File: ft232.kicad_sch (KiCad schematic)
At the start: 0 parts

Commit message: Add components: TXS0108E, FT232 oscillators/power/USB, symbol library table
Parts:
- added C16: 100nf, Capacitor_SMD:C_0805_2012Metric, symbol Device:C
- added C17, C18: 33nf, Capacitor_SMD:C_0805_2012Metric, symbol Device:C
- added D1, D2: RX, Diode_SMD:D_0805_2012Metric, symbol Device:LED_Small
- added J3: tp_ft232_, Library:connector_pin1, symbol Connector:Conn_01x01_Pin
- added Q1: 2N7002, Package_TO_SOT_SMD:SOT-23, symbol Transistor_FET:2N7002
- added R16, R17, R18, R19, R22, R23, R26: 10K, Resistor_SMD:R_0805_2012Metric, symbol Device:R
- added R20, R21: 100, Resistor_SMD:R_0805_2012Metric, symbol Device:R
- added R24, R25: 1K5, Resistor_SMD:R_0805_2012Metric, symbol Device:R
- added R27: 4K7, Resistor_SMD:R_0805_2012Metric, symbol Device:R
- added U3: FT232BM, Package_QFP:LQFP-32_7x7mm_P0.8mm, symbol Interface_USB:FT232BM
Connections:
- new net: C17.1, R24.1, U3.30 (AVCC)
- new net: D2.2 (A), R22.2
- new net: D1.2 (A), R19.2
- new net: R23.2, U3.10 (~{SLEEP})
- new net: D2.1 (K), U3.11 (~{RXLED})
- new net: C18.1, J3.1 (Pin_1), U3.6 (3V3OUT)
- new net: D1.1 (K), U3.12 (~{TXLED})
- new net: R21.1, U3.24 (D1/RXD)
- new net: R20.1, U3.25 (D0/TXD)
- new net: Q1.3 (D), R16.1
- new net: Q1.1 (G), R18.2
- new net +3V3: R19.1, R22.1, R23.1, U3.13 (VCCIO)
- new net FT: R17.2, U3.14 (PWRCTL)
- new net FT_CTS: C16.2, U3.22 (D3/~{CTS})
- new net FT_DCD: U3.19 (D6/~{DCD})
- new net FT_DRS: U3.20 (D5/~{DSR})
- new net FT_DTR: U3.21 (D4/~{DTR})
- new net FT_EECS: U3.32 (EECS)
- new net FT_EEDATA: U3.2 (EEDATA)
- new net FT_EESK: U3.1 (EESK)
- new net FT_PWR_EN: R18.1, U3.15 (~{PWREN})
- new net FT_RESET: R26.2, R27.2, U3.4 (~{RESET})
- new net FT_RI: U3.18 (D7/~{RI})
- new net FT_RST: U3.23 (D2/~{RST})
- new net FT_RST_OUT: R25.1, U3.5 (~{RSTOUT})
- new net FT_TXD_EN: U3.16 (TXDEN)
- new net FT_USB_BM: U3.8 (USBDM)
- new net FT_USB_DP: R25.2, U3.7 (USBDP)
- new net FT_XTIN: U3.27 (XTIN)
- new net FT_XTOUT: U3.28 (XTOUT)
- new net GND: C17.2, C18.2, Q1.2 (S), R17.1, R26.1, U3.17 (GND), U3.29 (AGND), U3.31 (TEST), U3.9 (GND)
- new net RX_MCU: R20.2
- new net TX_MCU: R21.2
- new net V+_USB: R16.2, R24.2, R27.1, U3.26 (VCC), U3.3 (VCC)
- new net mclr: C16.1
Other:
- added sheet osc_ft232 (osc_ft232.kicad_sch)
- added sheet power_ft232 (power_ft232.kicad_sch)
- added sheet tp_ft232 (tp_ft232.kicad_sch)
- added sheet usb_conector_Ft232 (usb_conector_Ft232.kicad_sch)

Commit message: ESP32S3 branch initial changes
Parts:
- added C21, C22: 15p, Capacitor_SMD:C_0805_2012Metric, symbol Device:C
- added C36, C39, C40, C41: 100nf, Capacitor_SMD:C_0805_2012Metric, symbol Device:C
- added J1: FT232, symbol Connector:Conn_01x06_Pin
- added R34: 10K, Resistor_SMD:R_0805_2012Metric, symbol Device:R
- added Y2: 6MHZ, Crystal:Crystal_SMD_0603-4Pin_6.0x3.5mm, symbol Device:Crystal_GND24
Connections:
- net +3V3: now also C36.1, C39.1, C40.2, C41.2, R34.1
- net FT_CTS: now also J1.5 (Pin_5)
- net FT_DTR: now also J1.1 (Pin_1)
- net FT_RESET: now also R34.2
- net FT_XTIN: now also C21.1, Y2.1
- net FT_XTOUT: now also C22.1, Y2.3
- net GND: now also C21.2, C22.2, C36.2, C39.2, C40.1, C41.1, J1.6 (Pin_6), Y2.2, Y2.4
- net V+_USB: now also J1.4 (Pin_4)
- net RX_MCU renamed FT_TX
- net FT_TX: now also J1.2 (Pin_2)
- net TX_MCU renamed FT_RX
- net FT_RX: now also J1.3 (Pin_3)
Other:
- removed sheet osc_ft232
- removed sheet power_ft232
- removed sheet tp_ft232
- moved on the sheet: C16, C17, C18, D1, D2, J3, Q1, R16, R17, R18, R19, R20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

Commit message: Update KiCad project files
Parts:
- removed Y2: 6MHZ, Crystal:Crystal_SMD_0603-4Pin_6.0x3.5mm, symbol Device:Crystal_GND24
- added C10, C13, C14: 100n, Capacitor_SMD:C_0402_1005Metric, symbol Device:C
- added C17, C18: 100nf, Capacitor_SMD:C_0805_2012Metric, symbol Device:C
- added C8: 33nf, symbol Device:C
- added J3: USB_B_Mini, kiC:USB_Mini-B_Lumberg_2486_01_Horizontal, symbol Connector:USB_B_Mini
- added J4: tp_ft232_, Library:connector_pin1, symbol Connector:Conn_01x01_Pin
- added JP1: Jumper_2_Open, Jumper:SolderJumper-2_P1.3mm_Open_RoundedPad1.0x1.5mm, symbol Jumper:Jumper_2_Open
- added L1: 100mh, Inductor_SMD:L_1206_3216Metric, symbol Device:L
- added Q1, Q3: BC847, symbol Transistor_BJT:BC847
- added Q4, Q5: Q_NPN_BCE, Package_TO_SOT_SMD:SOT-23W, symbol Device:Q_NPN_BCE
- added R1, R3, R9: 0, symbol Device:R
- added R15, R16, R20: 10k, Resistor_SMD:R_0402_1005Metric, symbol Device:R
- added R22, R23: 27, Resistor_SMD:R_0805_2012Metric, symbol Device:R
- added R4, R5: 10K, symbol Device:R
- added SW1, SW2: SW_Push, Button_Switch_SMD:SW_Push_SPST_NO_Alps_SKRK, symbol Switch:SW_Push
- added U4: LM1117DT-3.3, Package_TO_SOT_SMD:TO-252-3_TabPin2, symbol Regulator_Linear:LM1117DT-3.3
- added Y1: Crystal, Crystal:Resonator-2Pin_W10.0mm_H5.0mm, symbol Device:Crystal
- J1: value FT232 -> FT232RL; footprint (none) -> Connector_PinHeader_2.54mm:PinHeader_1x06_P2.54mm_Vertical
- renumbered C17 to C11, C18 to C12, C21 to C15, C22 to C16, C36 to C4, C39 to C5, C40 to C6, C41 to C7, C16 to C9, J3 to J2, Q1 to Q2, R20 to R10, R21 to R11, R22 to R12, R23 to R13, R24 to R14, R25 to R17, R34 to R18, R26 to R19, R16 to R2, R27 to R21, R17 to R6, R18 to R7, R19 to R8
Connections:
- net +3V3: now also C18.2, U4.2 (VO)
- net FT_DTR: now also Q5.3 (E), R15.1
- net FT_RST: now also Q4.3 (E), R16.1
- net FT_USB_BM: now also R23.1
- net FT_USB_DP: now also R22.1
- net FT_XTIN: now also Y1.1
- net FT_XTOUT: now also Y1.2
- net GND: now also C10.2, C13.2, C14.2, C17.1, C18.1, C8.2, J3.5 (GND), J3.6 (Shield), SW1.1, SW2.1, U4.1 (GND)
- net V+_USB: now also C17.2, J4.1 (Pin_1), JP1.1 (A), L1.2, U4.3 (VI)
- new net: Q4.1 (B), R15.2
- new net: Q3.3 (C), R9.2
- new net: J3.1 (VBUS), L1.1
- new net: J3.2 (D-), R23.2
- new net: J3.3 (D+), R22.2
- new net: Q3.2 (E), R5.1
- new net: C8.1, R1.1, R5.2
- new net: Q3.1 (B), R4.2
- new net: Q5.1 (B), R16.2
- new net: Q1.1 (B), R1.2
- new net: Q1.2 (E), R4.1
- new net: Q1.3 (C), R3.2
- new net +3.3V: R20.1
- new net FT_VCC: JP1.2 (B)
- new net GPIO9: R9.1
- new net to_CHIP_PU: R3.1
- new net to_GPIO_0: C13.1, Q5.2 (C), SW2.2
- new net to_GPIO_EN: C10.1, C14.1, Q4.2 (C), R20.2, SW1.2
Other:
- removed sheet usb_conector_Ft232
- note added: "Automatic Bootloader"
- note added: "DTR RTS -> EN IO9 1 1 1 1 0 0 1 1 1 0 0 1 0 1 1 0"
- moved on the sheet: C4, C5, C6, C7

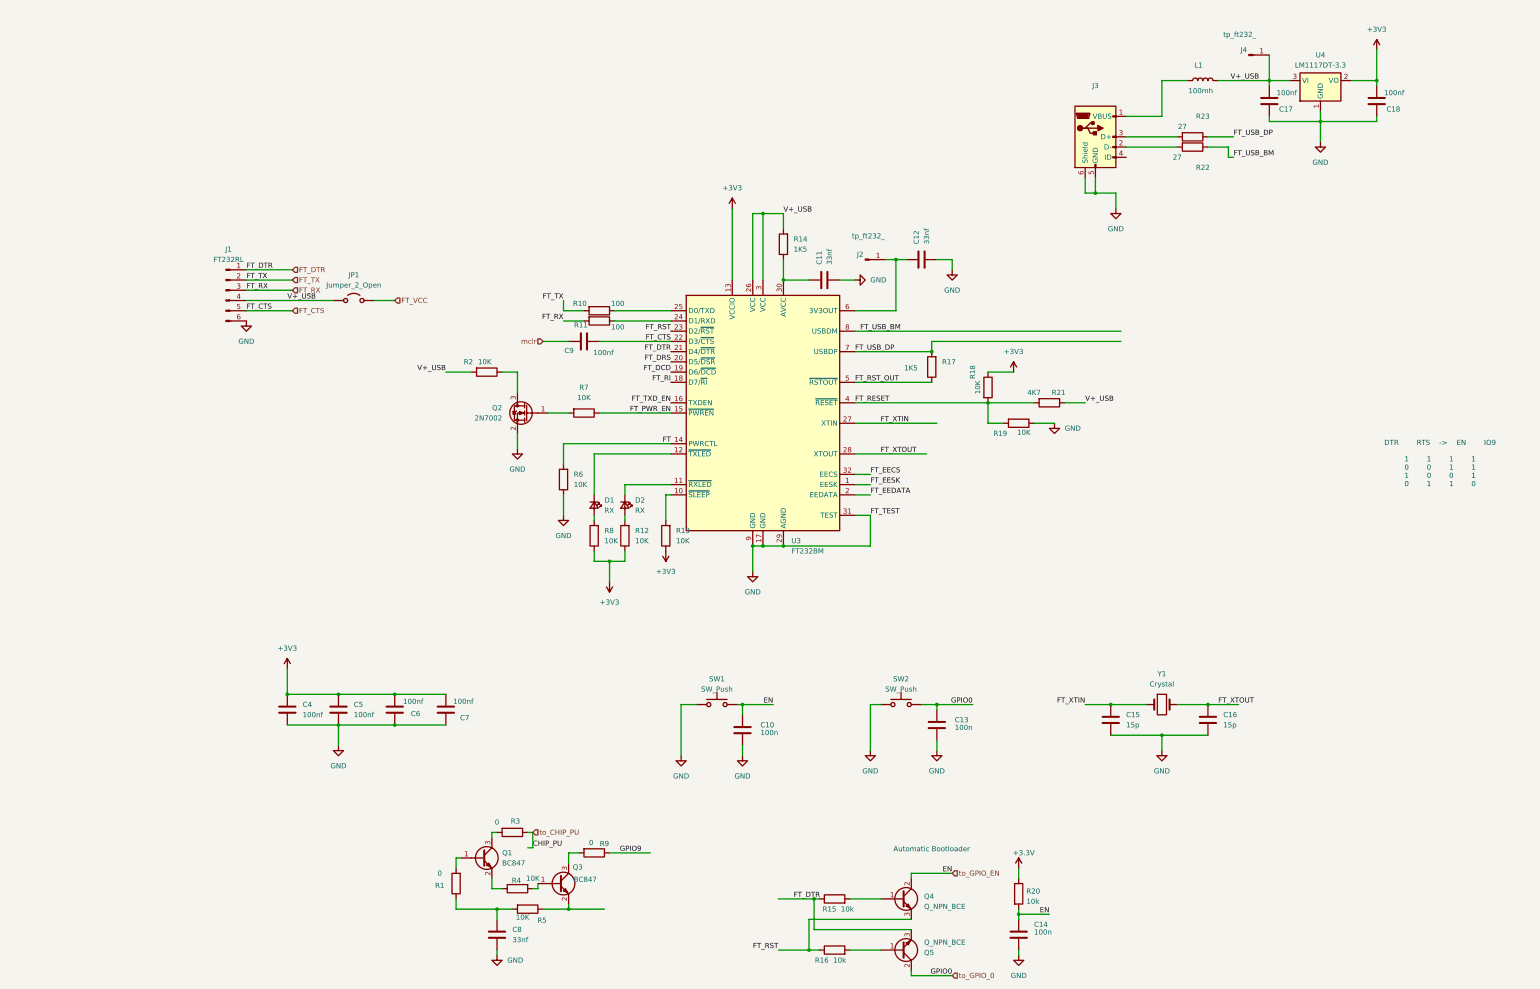
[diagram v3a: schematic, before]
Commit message: Rename +3V3 to +3.3VA in ft232 schematic
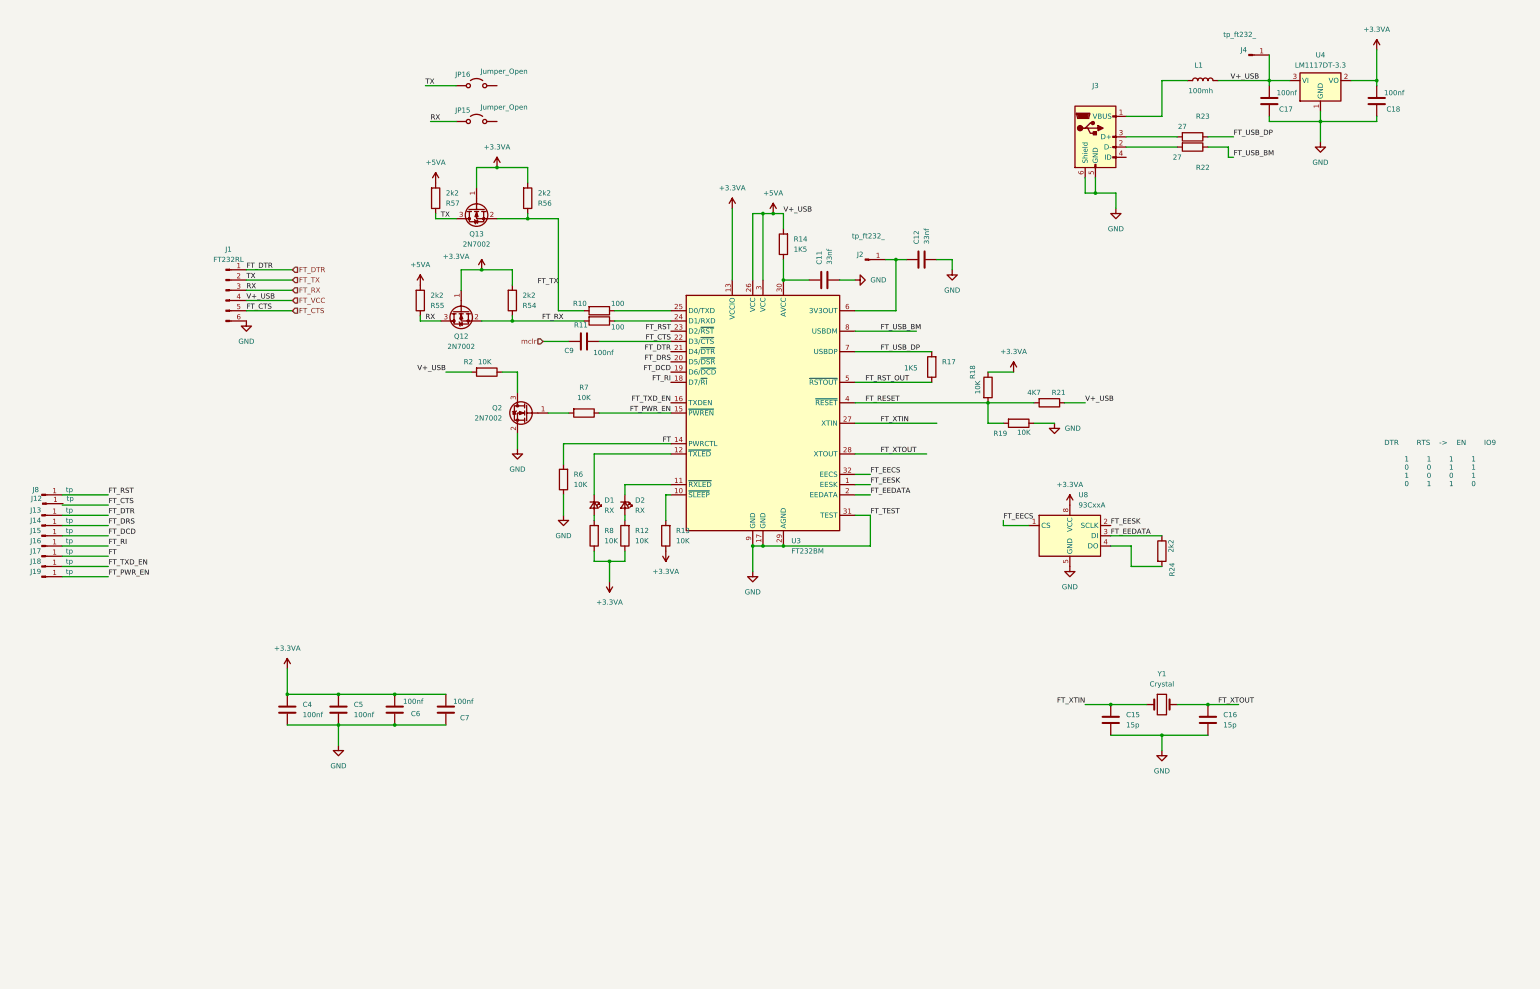
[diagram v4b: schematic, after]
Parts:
- removed C10, C13, C14: 100n, Capacitor_SMD:C_0402_1005Metric, symbol Device:C
- removed C8: 33nf, symbol Device:C
- removed JP1: Jumper_2_Open, Jumper:SolderJumper-2_P1.3mm_Open_RoundedPad1.0x1.5mm, symbol Jumper:Jumper_2_Open
- removed Q1, Q3: BC847, symbol Transistor_BJT:BC847
- removed Q4, Q5: Q_NPN_BCE, Package_TO_SOT_SMD:SOT-23W, symbol Device:Q_NPN_BCE
- removed R1, R3, R9: 0, symbol Device:R
- removed R15, R16, R20: 10k, Resistor_SMD:R_0402_1005Metric, symbol Device:R
- removed R4, R5: 10K, symbol Device:R
- removed SW1, SW2: SW_Push, Button_Switch_SMD:SW_Push_SPST_NO_Alps_SKRK, symbol Switch:SW_Push
- added J12, J13, J14, J15, J16, J17, J18, J19, J8: tp, TestPoint:TestPoint_Pad_D1.5mm, symbol Connector:Conn_01x01_Pin
- added JP15, JP16: Jumper_Open, Jumper:SolderJumper-2_P1.3mm_Open_RoundedPad1.0x1.5mm, symbol Jumper:Jumper_2_Open
- added Q12, Q13: 2N7002, Package_TO_SOT_SMD:SOT-23, symbol Transistor_FET:2N7002
- added R24, R54, R55, R56, R57: 2k2, Resistor_SMD:R_0805_2012Metric, symbol Device:R
- added U8: 93CxxA, Package_SO:SOIC-8_5.3x5.3mm_P1.27mm, symbol Memory_EEPROM:93CxxA
- R2, R7: footprint Resistor_SMD:R_0805_2012Metric -> Resistor_SMD:R_0603_1608Metric
- U4: footprint Package_TO_SOT_SMD:TO-252-3_TabPin2 -> kiC:SOT-223-3_TabPin2
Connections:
- net FT: now also J17.1 (Pin_1)
- net FT_DCD: now also J15.1 (Pin_1)
- net FT_DRS: now also J14.1 (Pin_1)
- net FT_DTR: now also J13.1 (Pin_1)
- net FT_EECS: now also U8.1 (CS)
- net FT_EEDATA: now also R24.1, U8.3 (DI)
- net FT_EESK: now also U8.2 (SCLK)
- net FT_PWR_EN: now also J19.1 (Pin_1)
- net FT_RI: now also J16.1 (Pin_1)
- net FT_RST: now also J8.1 (Pin_1)
- net FT_RX: now also JP15.1 (A), Q12.2 (S), Q12.3 (D), R54.1, R55.1
- net FT_TX: now also JP16.1 (A), Q13.2 (S), Q13.3 (D), R56.1, R57.1
- net FT_TXD_EN: now also J18.1 (Pin_1)
- net GND: now also U8.5 (GND)
- net +3V3 renamed +3.3VA
- net +3.3VA: now also Q12.1 (G), Q13.1 (G), R54.2, R56.2, U8.8 (VCC)
- net V+_USB renamed +5VA
- net +5VA: now also R55.2, R57.2
- new net: R24.2, U8.4 (DO)
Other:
- note removed: "Automatic Bootloader"

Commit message: Remove unused schematic files, lock files, and backup directories
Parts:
- removed Q2: 2N7002, Package_TO_SOT_SMD:SOT-23, symbol Transistor_FET:2N7002
- removed R2: 10K, Resistor_SMD:R_0603_1608Metric, symbol Device:R
- added C47, C48: 100nf, Capacitor_SMD:C_0805_2012Metric, symbol Device:C
- added J20: tp, TestPoint:TestPoint_THTPad_2.0x2.0mm_Drill1.0mm, symbol Connector:Conn_01x01_Pin
- added Q14: FDN306P, Package_TO_SOT_SMD:SOT-23W, symbol FDN306P:FDN306P
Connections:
- net +5VA: now also C47.2, C48.2, Q14.2
- net FT: no longer R6.2, U3.14 (PWRCTL)
- net GND: now also C48.1; no longer C11.2, C12.2, C4.2, C5.2, C6.1, C7.1
- net pwr_en: now reaches R7.2
- net pwr_en: now also C47.1, Q14.1
- new net FT_CTL: R6.2, U3.14 (PWRCTL)
- new net GND1: C11.2, C12.2, C4.2, C5.2, C6.1, C7.1
- new net PWR: J20.1 (Pin_1), Q14.3

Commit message: Update all schematic files and project
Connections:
- net ID: now reaches J3.4 (ID)
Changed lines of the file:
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@@
+	(wire
+		(pts
+			(xy 302.26 68.58) (xy 297.18 68.58)
+		)
+		(stroke
+			(width 0)
+			(type default)
+		)
+	)
 	(wire
 		(pts
@@
 		(effects
 			(font
+				(size 1.27 1.27)
+			)
+			(justify left bottom)
+		)
+	)
+	(label "ID"
+		(at 302.26 68.58 0)
+		(effects
+			(font

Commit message: Update all schematic files and project
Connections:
- net mclr renamed MCLR
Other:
- moved on the sheet: C15, C16, Y1
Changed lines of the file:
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@@
 	(text "DTR		RTS	->	EN		IO9\n\n1		1		1		1\n0		0		1		1\n1		0		0		1\n0		1		1		0\n"
 		(exclude_from_sim no)
-		(at 375.158 144.78 0)
+		(at 342.646 136.398 0)
 		(effects
 			(font
@@
 	)
 	(junction
-		(at 293.37 204.47)
+		(at 207.01 200.66)
 		(diameter 0)
 		(color 0 0 0 0)
@@
 	)
 	(junction
-		(at 317.5 204.47)
+		(at 231.14 200.66)
 		(diameter 0)
 		(color 0 0 0 0)
@@
 	)
 	(junction
-		(at 306.07 212.09)
+		(at 219.71 208.28)
 		(diameter 0)
 		(color 0 0 0 0)
@@
 	(wire
 		(pts
-			(xy 317.5 204.47) (xy 325.12 204.47)
+			(xy 231.14 200.66) (xy 238.76 200.66)
 		)
 		(stroke
@@
 	(wire
 		(pts
-			(xy 309.88 204.47) (xy 317.5 204.47)
+			(xy 223.52 200.66) (xy 231.14 200.66)
 		)
 		(stroke
@@
 	(wire
 		(pts
-			(xy 287.02 204.47) (xy 293.37 204.47)
+			(xy 200.66 200.66) (xy 207.01 200.66)
 		)
 		(stroke
@@
 	(wire
 		(pts
-			(xy 293.37 212.09) (xy 306.07 212.09)
+			(xy 207.01 208.28) (xy 219.71 208.28)
 		)
 		(stroke
@@
 	(wire
 		(pts
-			(xy 306.07 212.09) (xy 306.07 215.9)
+			(xy 219.71 208.28) (xy 219.71 212.09)
 		)
 		(stroke
@@
 	(wire
 		(pts
-			(xy 293.37 204.47) (xy 302.26 204.47)
+			(xy 207.01 200.66) (xy 215.9 200.66)
 		)
 		(stroke
@@
 	(wire
 		(pts
-			(xy 306.07 212.09) (xy 317.5 212.09)
+			(xy 219.71 208.28) (xy 231.14 208.28)
 		)
 		(stroke
@@
 		)
 	)
+	(label "MCLR"
+		(at 153.67 114.3 0)
+		(effects
+			(font
+				(size 1.27 1.27)
+			)
+			(justify left bottom)
+		)
+	)
 	(label "RX"
 		(at 123.19 109.22 0)
@@
 	)
 	(label "FT_XTOUT"
-		(at 320.04 204.47 0)
+		(at 233.68 200.66 0)
 		(effects
 			(font
@@
 	)
 	(label "FT_XTIN"
-		(at 287.02 204.47 180)
+		(at 200.66 200.66 180)
 		(effects
 			(font
@@
 		)
 	)
-	(hierarchical_label "mclr"
-		(shape input)
-		(at 152.4 114.3 180)
-		(effects
-			(font
-				(size 1.27 1.27)
-			)
-			(justify right)
-		)
-	)
 	(hierarchical_label "FT_DTR"
 		(shape input)
@@
 	(symbol
 		(lib_id "power:GND1")
-		(at 306.07 215.9 0)
+		(at 219.71 212.09 0)
 		(unit 1)
 		(body_style 1)
@@
 		(dnp no)
 		(property "Reference" "#PWR033"
-			(at 306.07 222.25 0)
+			(at 219.71 218.44 0)
 			(hide yes)
 			(show_name no)
@@
 		)
 		(property "Value" "GND"
-			(at 306.07 220.98 0)
+			(at 219.71 217.17 0)
 			(show_name no)
 			(do_not_autoplace no)
@@
 		)
 		(property "Footprint" ""
-			(at 306.07 215.9 0)
+			(at 219.71 212.09 0)
 			(hide yes)
 			(show_name no)
@@
 		)
 		(property "Datasheet" ""
-			(at 306.07 215.9 0)
+			(at 219.71 212.09 0)
 			(hide yes)
 			(show_name no)
@@
 		)
 		(property "Description" ""
-			(at 306.07 215.9 0)
+			(at 219.71 212.09 0)
 			(show_name no)
 			(do_not_autoplace no)
@@
 	(symbol
 		(lib_id "Device:Crystal")
-		(at 306.07 204.47 0)
+		(at 219.71 200.66 0)
 		(unit 1)
 		(body_style 1)
@@
 		(fields_autoplaced yes)
 		(property "Reference" "Y1"
-			(at 306.07 196.85 0)
+			(at 219.71 193.04 0)
 			(show_name no)
 			(do_not_autoplace no)
@@
 		)
 		(property "Value" "Crystal"
-			(at 306.07 199.39 0)
+			(at 219.71 195.58 0)
 			(show_name no)
 			(do_not_autoplace no)
@@
 		)
 		(property "Footprint" "Crystal:Resonator-2Pin_W10.0mm_H5.0mm"
-			(at 306.07 204.47 0)
+			(at 219.71 200.66 0)
 			(hide yes)
 			(show_name no)
@@
 		)
 		(property "Datasheet" ""
-			(at 306.07 204.47 0)
+			(at 219.71 200.66 0)
 			(hide yes)
 			(show_name no)
@@
 		)
 		(property "Description" "Two pin crystal"
-			(at 306.07 204.47 0)
+			(at 219.71 200.66 0)
 			(hide yes)
 			(show_name no)
@@
 	(symbol
 		(lib_id "Device:C")
-		(at 317.5 208.28 0)
+		(at 231.14 204.47 0)
 		(unit 1)
 		(body_style 1)
@@
 		(dnp no)
 		(property "Reference" "C16"
-			(at 321.31 207.01 0)
+			(at 234.95 203.2 0)
 			(show_name no)
 			(do_not_autoplace no)
@@
 		)
 		(property "Value" "15p"
-			(at 321.31 209.55 0)
+			(at 234.95 205.74 0)
 			(show_name no)
 			(do_not_autoplace no)
@@
 		)
 		(property "Footprint" "Capacitor_SMD:C_0805_2012Metric"
-			(at 318.4652 212.09 0)
+			(at 232.1052 208.28 0)
 			(hide yes)
 			(show_name no)
@@
 		)
 		(property "Datasheet" ""
-			(at 317.5 208.28 0)
+			(at 231.14 204.47 0)
 			(hide yes)
 			(show_name no)
@@
 		)
 		(property "Description" ""
-			(at 317.5 208.28 0)
+			(at 231.14 204.47 0)
 			(show_name no)
 			(do_not_autoplace no)
@@
 	(symbol
 		(lib_id "Device:C")
-		(at 293.37 208.28 0)
+		(at 207.01 204.47 0)
 		(unit 1)
 		(body_style 1)
@@
 		(dnp no)
 		(property "Reference" "C15"
-			(at 297.18 207.01 0)
+			(at 210.82 203.2 0)
 			(show_name no)
 			(do_not_autoplace no)
@@
 		)
 		(property "Value" "15p"
-			(at 297.18 209.55 0)
+			(at 210.82 205.74 0)
 			(show_name no)
 			(do_not_autoplace no)
@@
 		)
 		(property "Footprint" "Capacitor_SMD:C_0805_2012Metric"
-			(at 294.3352 212.09 0)
+			(at 207.9752 208.28 0)
 			(hide yes)
 			(show_name no)
@@
 		)
 		(property "Datasheet" ""
-			(at 293.37 208.28 0)
+			(at 207.01 204.47 0)
 			(hide yes)
 			(show_name no)
@@
 		)
 		(property "Description" ""
-			(at 293.37 208.28 0)
+			(at 207.01 204.47 0)
 			(show_name no)
 			(do_not_autoplace no)
